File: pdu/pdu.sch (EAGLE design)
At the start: 58 parts, among them IC1 FDN359BN, IC2 FDN359BN, IC3 FDN359BN, J1 S2B-PH-K-S(LF)(SN), J10 S2B-PH-K-S(LF)(SN), J2 S2B-PH-K-S(LF)(SN), J3 S2B-PH-K-S(LF)(SN), J4 S2B-PH-K-S(LF)(SN), J5 S2B-PH-K-S(LF)(SN), J6 S2B-PH-K-S(LF)(SN), J7 S2B-PH-K-S(LF)(SN), J8 S2B-PH-K-S(LF)(SN), J9 S2B-PH-K-S(LF)(SN)

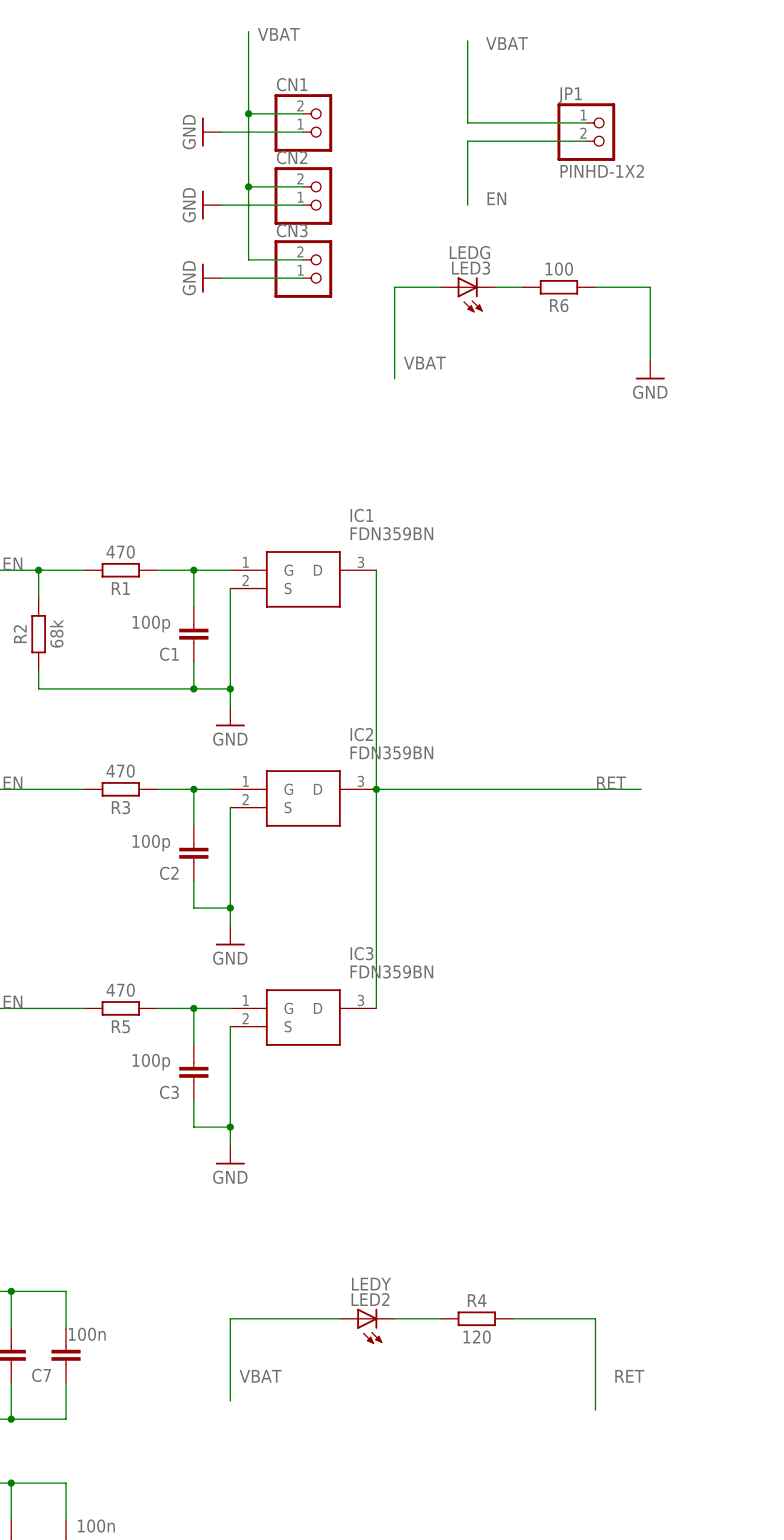
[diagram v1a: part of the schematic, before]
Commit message: add test pads
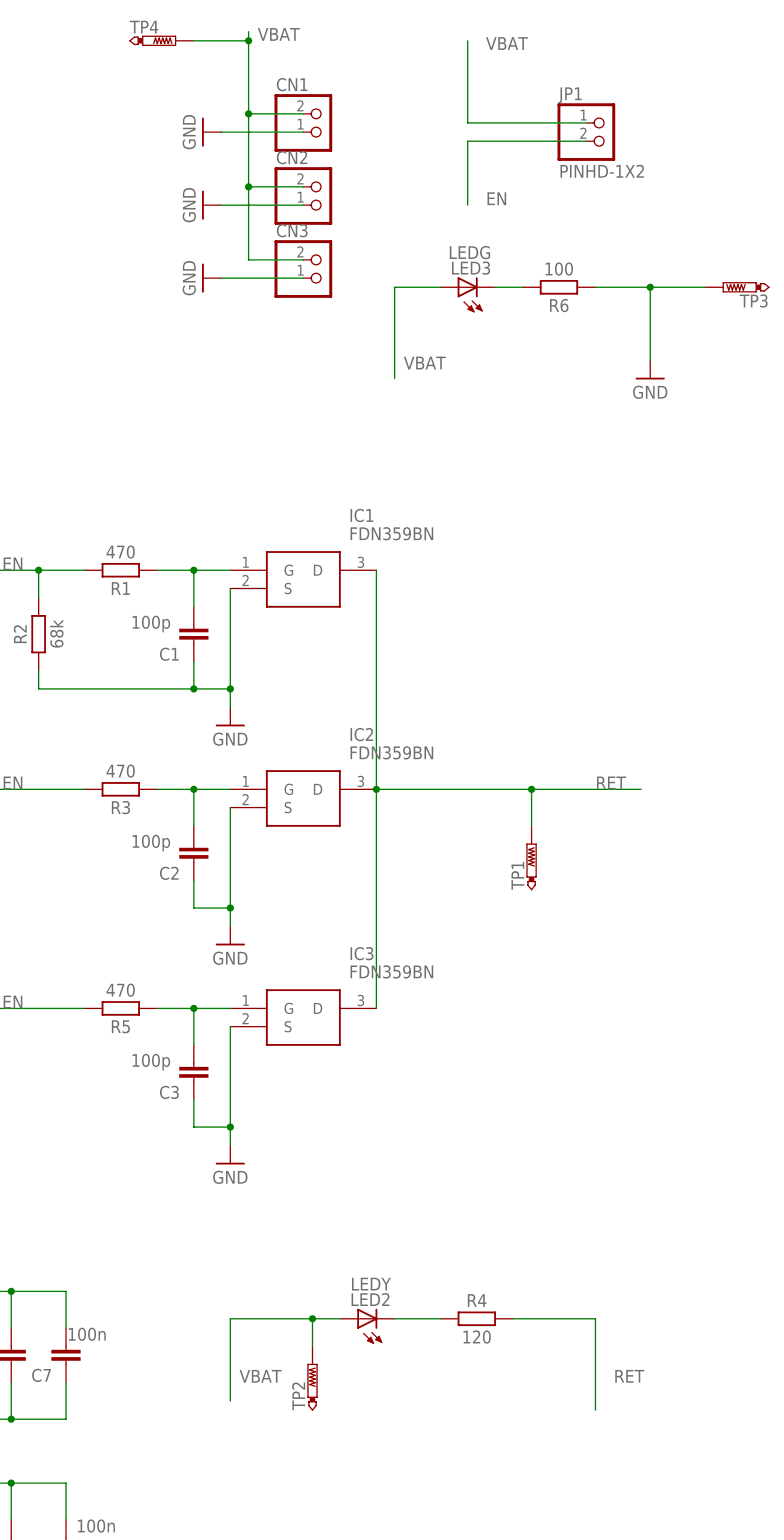
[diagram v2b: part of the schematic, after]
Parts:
- added TP1, TP2, TP3, TP4: PTR1PAD1-13, testpad:PTR1PAD1-13
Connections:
- net GND: now also TP3.TP
- net RET: now also TP1.TP
- net VBAT: now also TP2.TP, TP4.TP
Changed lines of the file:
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@@
 <parts>
 <part name="CN1" library="adafruit" library_urn="urn:adsk.eagle:library:420" deviceset="JST_2PIN" device="-THM-RA" package3d_urn="urn:adsk.eagle:package:6240694/1" override_package3d_urn="urn:adsk.eagle:package:44326866/2" override_package_urn="urn:adsk.eagle:footprint:6240048/1"/>
-<part name="CN2" library="adafruit" library_urn="urn:adsk.eagle:library:420" deviceset="JST_2PIN" device="-THM-RA" package3d_urn="urn:adsk.eagle:package:6240694/1"/>
-<part name="CN3" library="adafruit" library_urn="urn:adsk.eagle:library:420" deviceset="JST_2PIN" device="-THM-RA" package3d_urn="urn:adsk.eagle:package:6240694/1"/>
+<part name="CN2" library="adafruit" library_urn="urn:adsk.eagle:library:420" deviceset="JST_2PIN" device="-THM-RA" package3d_urn="urn:adsk.eagle:package:6240694/1" override_package3d_urn="urn:adsk.eagle:package:44326871/2" override_package_urn="urn:adsk.eagle:footprint:6240048/1"/>
+<part name="CN3" library="adafruit" library_urn="urn:adsk.eagle:library:420" deviceset="JST_2PIN" device="-THM-RA" package3d_urn="urn:adsk.eagle:package:6240694/1" override_package3d_urn="urn:adsk.eagle:package:44326874/2" override_package_urn="urn:adsk.eagle:footprint:6240048/1"/>
 <part name="SUPPLY1" library="Power_Symbols" library_urn="urn:adsk.eagle:library:16502351" deviceset="GND-BAR" device="" value="GND"/>
 <part name="SUPPLY2" library="Power_Symbols" library_urn="urn:adsk.eagle:library:16502351" deviceset="GND-BAR" device="" value="GND"/>
@@
 <part name="SUPPLY4" library="Power_Symbols" library_urn="urn:adsk.eagle:library:16502351" deviceset="GND-BAR" device="" value="GND"/>
 <part name="C1" library="Capacitor" library_urn="urn:adsk.eagle:library:16290819" deviceset="C" device="CHIP-0603(1608-METRIC)" package3d_urn="urn:adsk.eagle:package:16290898/5" technology="_" value="100p"/>
-<part name="IC2" library="SamacSys_Parts" deviceset="FDN359BN" device=""/>
+<part name="IC2" library="SamacSys_Parts" deviceset="FDN359BN" device="" override_package3d_urn="urn:adsk.eagle:package:44326876/2" override_package_urn="urn:adsk.eagle:footprint:44326877/1"/>
 <part name="R3" library="Resistor" library_urn="urn:adsk.eagle:library:16378527" deviceset="R" device="CHIP-0603(1608-METRIC)" package3d_urn="urn:adsk.eagle:package:16378565/5" technology="_" value="470"/>
 <part name="SUPPLY5" library="Power_Symbols" library_urn="urn:adsk.eagle:library:16502351" deviceset="GND-BAR" device="" value="GND"/>
 <part name="C2" library="Capacitor" library_urn="urn:adsk.eagle:library:16290819" deviceset="C" device="CHIP-0603(1608-METRIC)" package3d_urn="urn:adsk.eagle:package:16290898/5" technology="_" value="100p"/>
-<part name="IC3" library="SamacSys_Parts" deviceset="FDN359BN" device=""/>
+<part name="IC3" library="SamacSys_Parts" deviceset="FDN359BN" device="" override_package3d_urn="urn:adsk.eagle:package:44326879/2" override_package_urn="urn:adsk.eagle:footprint:44326880/1"/>
 <part name="R5" library="Resistor" library_urn="urn:adsk.eagle:library:16378527" deviceset="R" device="CHIP-0603(1608-METRIC)" package3d_urn="urn:adsk.eagle:package:16378565/5" technology="_" value="470"/>
 <part name="SUPPLY6" library="Power_Symbols" library_urn="urn:adsk.eagle:library:16502351" deviceset="GND-BAR" device="" value="GND"/>
@@
 <part name="LED3" library="adafruit" library_urn="urn:adsk.eagle:library:420" deviceset="LED" device="CHIPLED_0805" package3d_urn="urn:adsk.eagle:package:6240559/1" value="LEDG"/>
 <part name="SUPPLY7" library="Power_Symbols" library_urn="urn:adsk.eagle:library:16502351" deviceset="GND-BAR" device="" value="GND"/>
+<part name="TP1" library="testpad" library_urn="urn:adsk.eagle:library:385" deviceset="PTR1" device="PAD1-13" package3d_urn="urn:adsk.eagle:package:27946/1"/>
+<part name="TP2" library="testpad" library_urn="urn:adsk.eagle:library:385" deviceset="PTR1" device="PAD1-13" package3d_urn="urn:adsk.eagle:package:27946/1"/>
+<part name="TP3" library="testpad" library_urn="urn:adsk.eagle:library:385" deviceset="PTR1" device="PAD1-13" package3d_urn="urn:adsk.eagle:package:27946/1"/>
+<part name="TP4" library="testpad" library_urn="urn:adsk.eagle:library:385" deviceset="PTR1" device="PAD1-13" package3d_urn="urn:adsk.eagle:package:27946/1"/>
 </parts>
 <sheets>
@@
 <instance part="SUPPLY7" gate="G$1" x="58.42" y="26.67" smashed="yes">
 <attribute name="VALUE" x="58.42" y="24.765" size="1.778" layer="96" align="center"/>
+</instance>
+<instance part="TP1" gate="G$1" x="41.91" y="-38.1" smashed="yes">
+<attribute name="NAME" x="40.894" y="-44.45" size="1.778" layer="95" rot="R90"/>
+<attribute name="TP_SIGNAL_NAME" x="43.18" y="-40.64" size="1.778" layer="97"/>
+</instance>
+<instance part="TP2" gate="G$1" x="11.43" y="-110.49" smashed="yes">
+<attribute name="NAME" x="10.414" y="-116.84" size="1.778" layer="95" rot="R90"/>
+<attribute name="TP_SIGNAL_NAME" x="12.7" y="-113.03" size="1.778" layer="97"/>
+</instance>
+<instance part="TP3" gate="G$1" x="68.58" y="39.37" smashed="yes" rot="R90">
+<attribute name="NAME" x="74.93" y="38.354" size="1.778" layer="95" rot="R180"/>
+<attribute name="TP_SIGNAL_NAME" x="71.12" y="40.64" size="1.778" layer="97" rot="R90"/>
+</instance>
+<instance part="TP4" gate="G$1" x="-7.62" y="73.66" smashed="yes" rot="R270">
+<attribute name="NAME" x="-13.97" y="74.676" size="1.778" layer="95"/>
+<attribute name="TP_SIGNAL_NAME" x="-10.16" y="72.39" size="1.778" layer="97" rot="R270"/>
 </instance>
 </instances>
@@
 <pinref part="SUPPLY7" gate="G$1" pin="GND"/>
 <wire x1="58.42" y1="39.37" x2="58.42" y2="29.21" width="0.1524" layer="91"/>
+<pinref part="TP3" gate="G$1" pin="TP"/>
+<wire x1="66.04" y1="39.37" x2="58.42" y2="39.37" width="0.1524" layer="91"/>
+<junction x="58.42" y="39.37"/>
 </segment>
 </net>
@@
 <pinref part="CN1" gate="G$1" pin="1"/>
 <wire x1="2.54" y1="53.34" x2="2.54" y2="63.5" width="0.1524" layer="91"/>
-<wire x1="2.54" y1="63.5" x2="2.54" y2="74.93" width="0.1524" layer="91"/>
+<wire x1="2.54" y1="63.5" x2="2.54" y2="73.66" width="0.1524" layer="91"/>
+<wire x1="2.54" y1="73.66" x2="2.54" y2="74.93" width="0.1524" layer="91"/>
 <wire x1="10.16" y1="63.5" x2="2.54" y2="63.5" width="0.1524" layer="91"/>
 <junction x="2.54" y="63.5"/>
@@
 <junction x="2.54" y="53.34"/>
 <label x="3.81" y="73.66" size="1.778" layer="95"/>
+<pinref part="TP4" gate="G$1" pin="TP"/>
+<wire x1="-5.08" y1="73.66" x2="2.54" y2="73.66" width="0.1524" layer="91"/>
+<junction x="2.54" y="73.66"/>
 </segment>
 <segment>
@@
 <segment>
 <pinref part="LED2" gate="G$1" pin="A"/>
-<wire x1="15.24" y1="-104.14" x2="0" y2="-104.14" width="0.1524" layer="91"/>
+<wire x1="15.24" y1="-104.14" x2="11.43" y2="-104.14" width="0.1524" layer="91"/>
+<wire x1="11.43" y1="-104.14" x2="0" y2="-104.14" width="0.1524" layer="91"/>
 <wire x1="0" y1="-104.14" x2="0" y2="-115.57" width="0.1524" layer="91"/>
 <label x="1.27" y="-113.03" size="1.778" layer="95"/>
+<pinref part="TP2" gate="G$1" pin="TP"/>
+<wire x1="11.43" y1="-107.95" x2="11.43" y2="-104.14" width="0.1524" layer="91"/>
+<junction x="11.43" y="-104.14"/>
 </segment>
 </net>
@@
 <wire x1="20.32" y1="-30.48" x2="20.32" y2="0" width="0.1524" layer="91"/>
 <junction x="20.32" y="-30.48"/>
-<wire x1="20.32" y1="-30.48" x2="57.15" y2="-30.48" width="0.1524" layer="91"/>
+<wire x1="20.32" y1="-30.48" x2="41.91" y2="-30.48" width="0.1524" layer="91"/>
 <label x="50.8" y="-30.48" size="1.778" layer="95"/>
-</segment>
-<segment>
+<pinref part="TP1" gate="G$1" pin="TP"/>
+<wire x1="41.91" y1="-30.48" x2="57.15" y2="-30.48" width="0.1524" layer="91"/>
+<wire x1="41.91" y1="-35.56" x2="41.91" y2="-30.48" width="0.1524" layer="91"/>
+<junction x="41.91" y="-30.48"/>
+</segment>
+<segment>
